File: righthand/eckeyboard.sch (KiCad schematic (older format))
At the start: 71 parts, among them J4 Conn_01x06_Male, J5 Conn_01x06_Male, U1 74HC4051, U2 NJM2742, U4 74LS138

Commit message: [fix] small fix
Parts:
- TP1, TP10, TP11, TP12, TP13, TP14, TP15, TP16, TP17, TP18, TP19, TP2, TP20, TP21, TP22, TP23, TP24, TP25, TP26, TP27, TP28, TP29, TP3, TP30, TP31, TP32, TP33, TP34, TP35, TP4, TP5, TP6, TP7, TP8, TP9: symbol TopreLib:ToprePad -> eckeyboard-rescue:ToprePad-TopreLib
- U2: symbol akzuki:NJM2742 -> eckeyboard-rescue:NJM2742-akzuki
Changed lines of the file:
@@
 $EndDescr
 $Comp
-L TopreLib:ToprePad TP2
+L eckeyboard-rescue:ToprePad-TopreLib TP2
 U 1 1 5E69A1C3
 P 4825 2500
@@
 $EndComp
 $Comp
-L TopreLib:ToprePad TP3
+L eckeyboard-rescue:ToprePad-TopreLib TP3
 U 1 1 5E69A1FD
 P 4825 2900
@@
 $EndComp
 $Comp
-L TopreLib:ToprePad TP6
+L eckeyboard-rescue:ToprePad-TopreLib TP6
 U 1 1 5E69A21E
 P 5225 2900
@@
 $EndComp
 $Comp
-L TopreLib:ToprePad TP1
+L eckeyboard-rescue:ToprePad-TopreLib TP1
 U 1 1 5E69A22F
 P 4825 2100
@@
 $EndComp
 $Comp
-L TopreLib:ToprePad TP9
+L eckeyboard-rescue:ToprePad-TopreLib TP9
 U 1 1 5E69A240
 P 5625 2900
@@
 $EndComp
 $Comp
-L TopreLib:ToprePad TP5
+L eckeyboard-rescue:ToprePad-TopreLib TP5
 U 1 1 5E69A261
 P 5225 2500
@@
 $EndComp
 $Comp
-L TopreLib:ToprePad TP4
+L eckeyboard-rescue:ToprePad-TopreLib TP4
 U 1 1 5E69A29A
 P 5225 2100
@@
 $EndComp
 $Comp
-L TopreLib:ToprePad TP8
+L eckeyboard-rescue:ToprePad-TopreLib TP8
 U 1 1 5E69A2B3
 P 5625 2500
@@
 $EndComp
 $Comp
-L TopreLib:ToprePad TP7
+L eckeyboard-rescue:ToprePad-TopreLib TP7
 U 1 1 5E69A2C4
 P 5625 2100
@@
 $EndComp
 $Comp
-L TopreLib:ToprePad TP10
+L eckeyboard-rescue:ToprePad-TopreLib TP10
 U 1 1 5E6A1DD9
 P 4825 3300
@@
 $EndComp
 $Comp
-L TopreLib:ToprePad TP12
+L eckeyboard-rescue:ToprePad-TopreLib TP12
 U 1 1 5E6A1DE2
 P 5225 3300
@@
 $EndComp
 $Comp
-L TopreLib:ToprePad TP14
+L eckeyboard-rescue:ToprePad-TopreLib TP14
 U 1 1 5E6A1DEB
 P 5625 3300
@@
 	5750 3400 5750 3000
 $Comp
-L TopreLib:ToprePad TP11
+L eckeyboard-rescue:ToprePad-TopreLib TP11
 U 1 1 5E6A3A9B
 P 4825 3700
@@
 $EndComp
 $Comp
-L TopreLib:ToprePad TP13
+L eckeyboard-rescue:ToprePad-TopreLib TP13
 U 1 1 5E6A3AA4
 P 5225 3700
@@
 Connection ~ 5450 3600
 $Comp
-L TopreLib:ToprePad TP17
+L eckeyboard-rescue:ToprePad-TopreLib TP17
 U 1 1 5E74D75A
 P 6025 2900
@@
 $EndComp
 $Comp
-L TopreLib:ToprePad TP16
+L eckeyboard-rescue:ToprePad-TopreLib TP16
 U 1 1 5E74D763
 P 6025 2500
@@
 $EndComp
 $Comp
-L TopreLib:ToprePad TP15
+L eckeyboard-rescue:ToprePad-TopreLib TP15
 U 1 1 5E74D76C
 P 6025 2100
@@
 Connection ~ 6150 2600
 $Comp
-L TopreLib:ToprePad TP18
+L eckeyboard-rescue:ToprePad-TopreLib TP18
 U 1 1 5E74D78A
 P 6025 3300
@@
 	6150 3400 6150 3000
 $Comp
-L TopreLib:ToprePad TP19
+L eckeyboard-rescue:ToprePad-TopreLib TP19
 U 1 1 5E74D79A
 P 6025 3700
@@
 Connection ~ 6250 3600
 $Comp
-L TopreLib:ToprePad TP22
+L eckeyboard-rescue:ToprePad-TopreLib TP22
 U 1 1 5E754EF5
 P 6425 2900
@@
 $EndComp
 $Comp
-L TopreLib:ToprePad TP21
+L eckeyboard-rescue:ToprePad-TopreLib TP21
 U 1 1 5E754EFE
 P 6425 2500
@@
 $EndComp
 $Comp
-L TopreLib:ToprePad TP20
+L eckeyboard-rescue:ToprePad-TopreLib TP20
 U 1 1 5E754F07
 P 6425 2100
@@
 Connection ~ 6550 2600
 $Comp
-L TopreLib:ToprePad TP23
+L eckeyboard-rescue:ToprePad-TopreLib TP23
 U 1 1 5E754F25
 P 6425 3300
@@
 	6800 4625 6800 4525
 $Comp
-L TopreLib:ToprePad TP26
+L eckeyboard-rescue:ToprePad-TopreLib TP26
 U 1 1 5E75FDBC
 P 6825 2900
@@
 $EndComp
 $Comp
-L TopreLib:ToprePad TP25
+L eckeyboard-rescue:ToprePad-TopreLib TP25
 U 1 1 5E75FDC5
 P 6825 2500
@@
 $EndComp
 $Comp
-L TopreLib:ToprePad TP24
+L eckeyboard-rescue:ToprePad-TopreLib TP24
 U 1 1 5E75FDCE
 P 6825 2100
@@
 Connection ~ 6950 2600
 $Comp
-L TopreLib:ToprePad TP27
+L eckeyboard-rescue:ToprePad-TopreLib TP27
 U 1 1 5E75FDEC
 P 6825 3300
@@
 $EndComp
 $Comp
-L akzuki:NJM2742 U2
+L eckeyboard-rescue:NJM2742-akzuki U2
 U 1 1 5E7249CA
 P 5175 6350
@@
 NoConn ~ 5675 6450
 $Comp
-L TopreLib:ToprePad TP28
+L eckeyboard-rescue:ToprePad-TopreLib TP28
 U 1 1 5E88EC5E
 P 6425 3700
@@
 	6650 3600 6650 4225
 $Comp
-L TopreLib:ToprePad TP31
+L eckeyboard-rescue:ToprePad-TopreLib TP31
 U 1 1 5E8F8111
 P 7225 2900
@@
 $EndComp
 $Comp
-L TopreLib:ToprePad TP30
+L eckeyboard-rescue:ToprePad-TopreLib TP30
 U 1 1 5E8F811A
 P 7225 2500
@@
 $EndComp
 $Comp
-L TopreLib:ToprePad TP29
+L eckeyboard-rescue:ToprePad-TopreLib TP29
 U 1 1 5E8F8123
 P 7225 2100
@@
 Connection ~ 7350 2600
 $Comp
-L TopreLib:ToprePad TP32
+L eckeyboard-rescue:ToprePad-TopreLib TP32
 U 1 1 5E8F813F
 P 7625 3300
@@
 	7450 4625 7450 4750
 $Comp
-L TopreLib:ToprePad TP35
+L eckeyboard-rescue:ToprePad-TopreLib TP35
 U 1 1 5E921A58
 P 7625 2900
@@
 $EndComp
 $Comp
-L TopreLib:ToprePad TP34
+L eckeyboard-rescue:ToprePad-TopreLib TP34
 U 1 1 5E921A61
 P 7625 2500
@@
 $EndComp
 $Comp
-L TopreLib:ToprePad TP33
+L eckeyboard-rescue:ToprePad-TopreLib TP33
 U 1 1 5E921A6A
 P 7625 2100

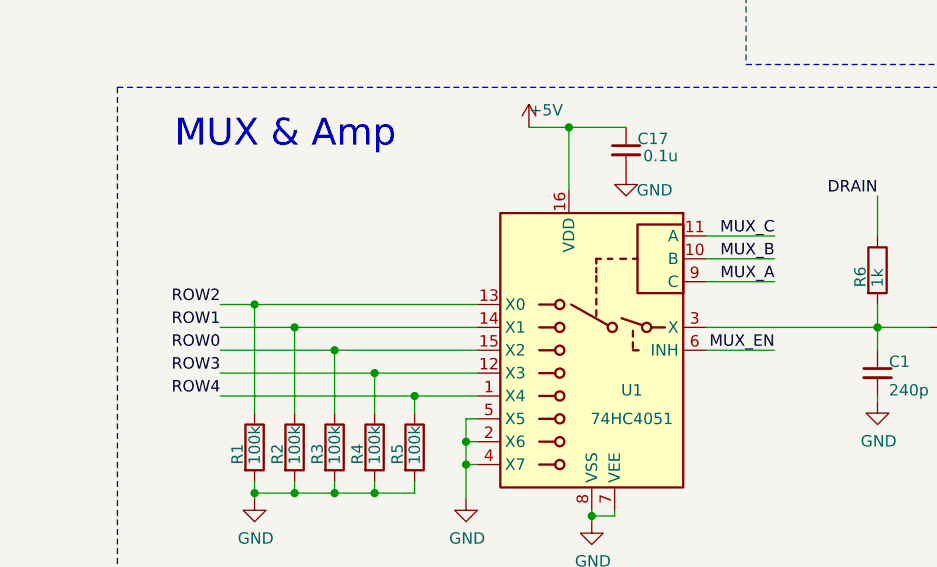
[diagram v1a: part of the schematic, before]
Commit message: [fix] MUX pin ordering fix
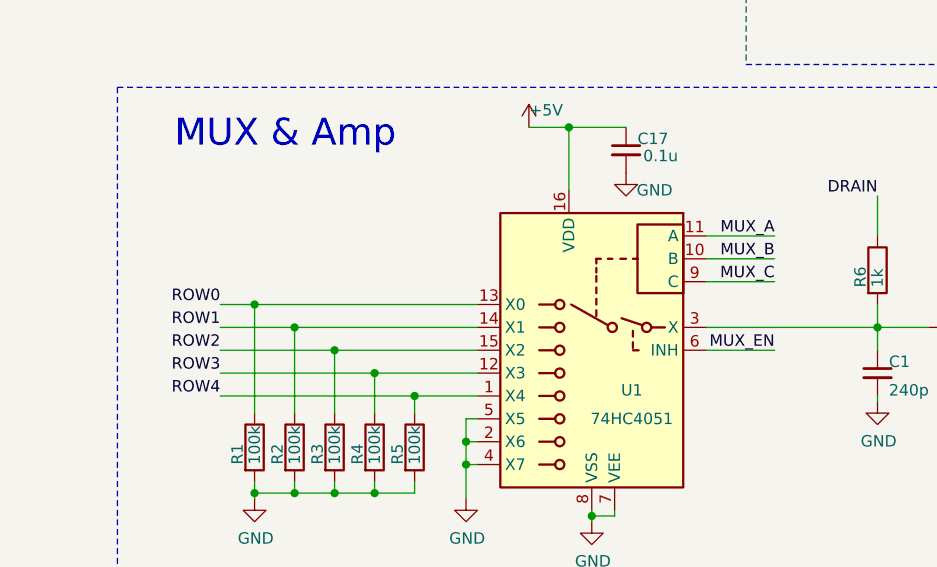
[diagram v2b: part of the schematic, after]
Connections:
- net MUX_A: now also U1.11 (A); no longer U1.9 (C)
- net MUX_C: now also U1.9 (C); no longer U1.11 (A)
- net ROW0: now also R1.1, U1.13 (X0); no longer R3.1, U1.15 (X2)
- net ROW2: now also R3.1, U1.15 (X2); no longer R1.1, U1.13 (X0)
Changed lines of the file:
@@
 Text Label 1500 6650 2    50   ~ 0
 ROW3
-Text Label 1500 6350 2    50   ~ 0
+Text Label 1500 6550 2    50   ~ 0
 ROW2
 Text Label 1500 6450 2    50   ~ 0
 ROW1
-Text Label 1500 6550 2    50   ~ 0
+Text Label 1500 6350 2    50   ~ 0
 ROW0
 $Comp
@@
 Wire Wire Line
 	9100 4650 9400 4650
-Text Label 3925 6250 2    50   ~ 0
+Text Label 3925 6050 2    50   ~ 0
 MUX_A
 Wire Wire Line
@@
 Text Label 3925 6150 2    50   ~ 0
 MUX_B
-Text Label 3925 6050 2    50   ~ 0
+Text Label 3925 6250 2    50   ~ 0
 MUX_C
 Wire Wire Line
